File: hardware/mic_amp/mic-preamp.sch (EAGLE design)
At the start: 16 parts

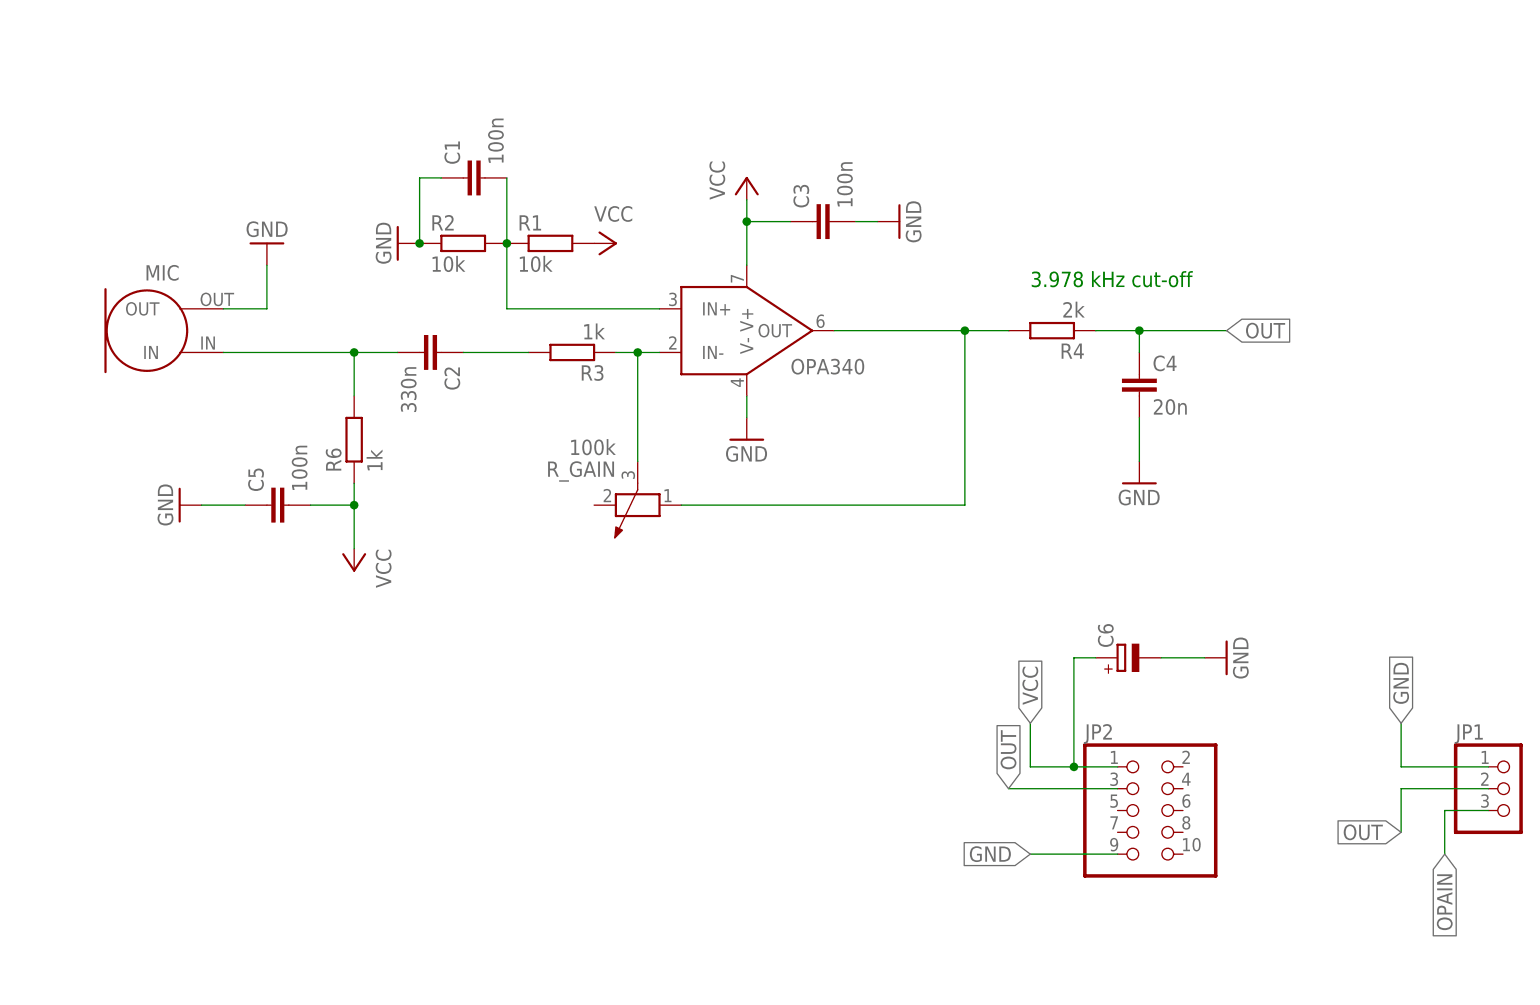
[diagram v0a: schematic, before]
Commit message: modified mic-amp for better noise immunity
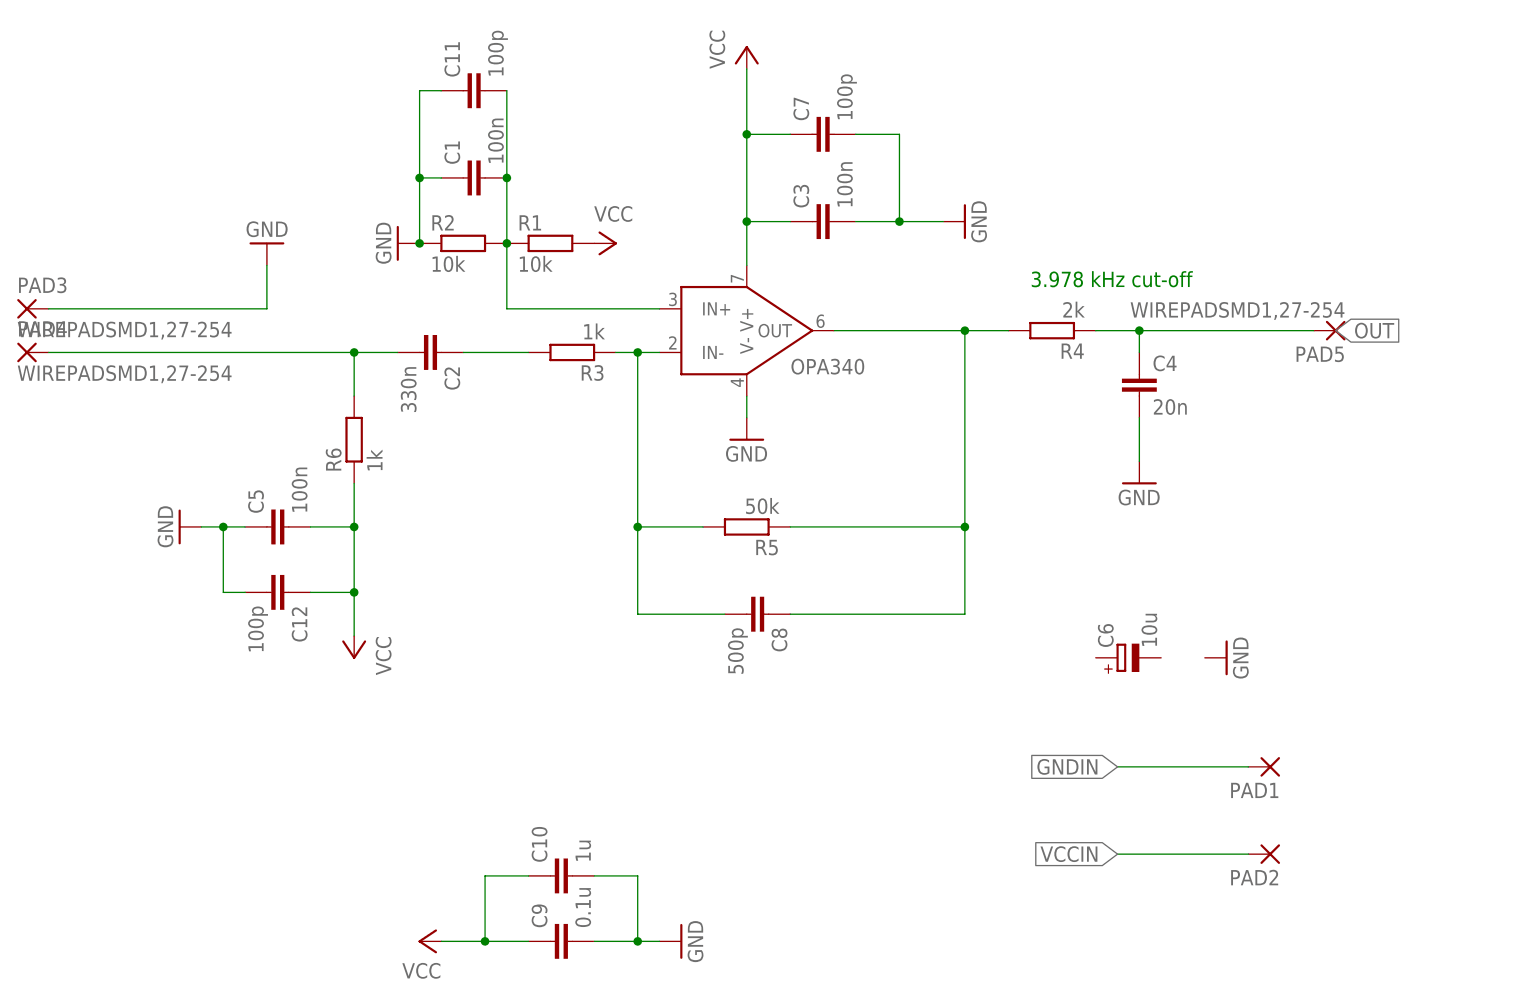
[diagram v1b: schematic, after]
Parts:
- removed JP1: (no value), pinhead:PINHD-1X3
- removed JP2: (no value), pinhead:PINHD-2X5
- removed MIC: MKD-1318, mic:MKD-1318
- removed R_GAIN: 100k, rcl:POTENTIOMETER_PT-10
- added C10: 1u, rcl:C-EUC0805
- added C11, C12, C7: 100p, rcl:C-EUC0805
- added C8: 500p, rcl:C-EUC0805
- added C9: 0.1u, rcl:C-EUC0805
- added PAD1, PAD2: WIREPADSMD2,54-5,08, wirepad:WIREPADSMD2,54-5,08
- added PAD3, PAD4, PAD5: WIREPADSMD1,27-254, wirepad:WIREPADSMD1,27-254
- added R5: 50k, rcl:R-EU_R0805
- C6: value (none) -> 10u
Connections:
- removed net OPAIN: JP1.3, OPA340.IN-, R3.1, R_GAIN.3
- new net GNDIN: PAD1.P
- new net N$5: C8.2, OPA340.IN-, R3.1, R5.2
- new net VCCIN: PAD2.P
- net GND: now also C10.2, C11.1, C12.2, C7.2, C9.2, PAD3.P; no longer C6.-, JP1.1, JP2.9, MIC.OUT
- net MIC: now also PAD4.P; no longer MIC.IN
- net N$1: now also C8.1, R5.1; no longer R_GAIN.1
- net N$2: now also C11.2
- net OUT: now also PAD5.P; no longer JP1.2, JP2.3
- net VCC: now also C10.1, C12.1, C7.1, C9.1; no longer C6.+, JP2.1
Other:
- moved on the sheet: C5
